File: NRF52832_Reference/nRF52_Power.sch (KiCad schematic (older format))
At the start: 37 parts

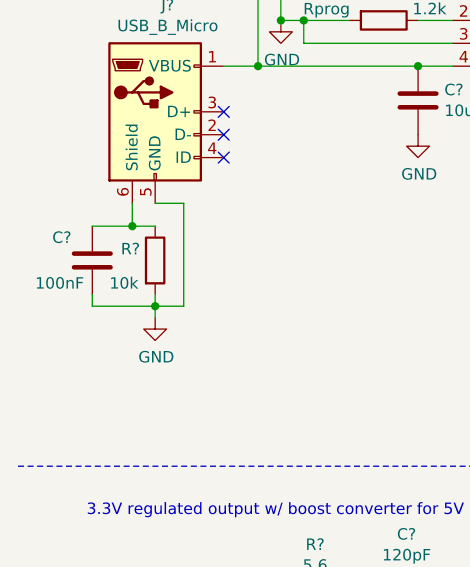
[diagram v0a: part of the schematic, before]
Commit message: Added footprint for LCD and finished footprint assignments for LCD components.
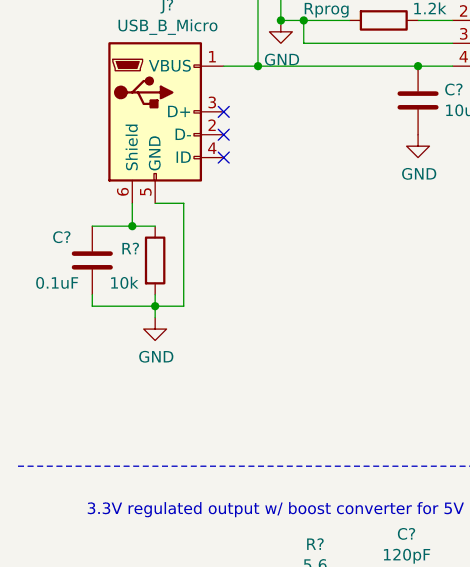
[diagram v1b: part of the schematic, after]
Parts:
- C?: value 100nF -> 0.1uF
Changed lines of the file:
@@
 P 825 3000
 F 0 "C?" H 650 3100 50  0000 L CNN
-F 1 "100nF" H 575 2900 50  0000 L CNN
+F 1 "0.1uF" H 575 2900 50  0000 L CNN
 F 2 "Capacitor_SMD:C_0603_1608Metric_Pad1.05x0.95mm_HandSolder" H 863 2850 50  0001 C CNN
 F 3 "~" H 825 3000 50  0001 C CNN

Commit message: Finished foorprint assignments for GPIO pins, LEDs, and button.
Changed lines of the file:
@@
 	0    1    1    0
 $EndComp
-Text Label 6200 2150 0    50   ~ 0
-V+
-Text Label 700  4900 0    50   ~ 0
-V+
 Wire Wire Line
 	1600 4900 1500 4900
@@
 Wire Wire Line
 	825  3200 1100 3200
+Text GLabel 6200 2150 2    50   Output ~ 0
+V+
+Text GLabel 700  4900 0    50   Input ~ 0
+V+
 $EndSCHEMATC

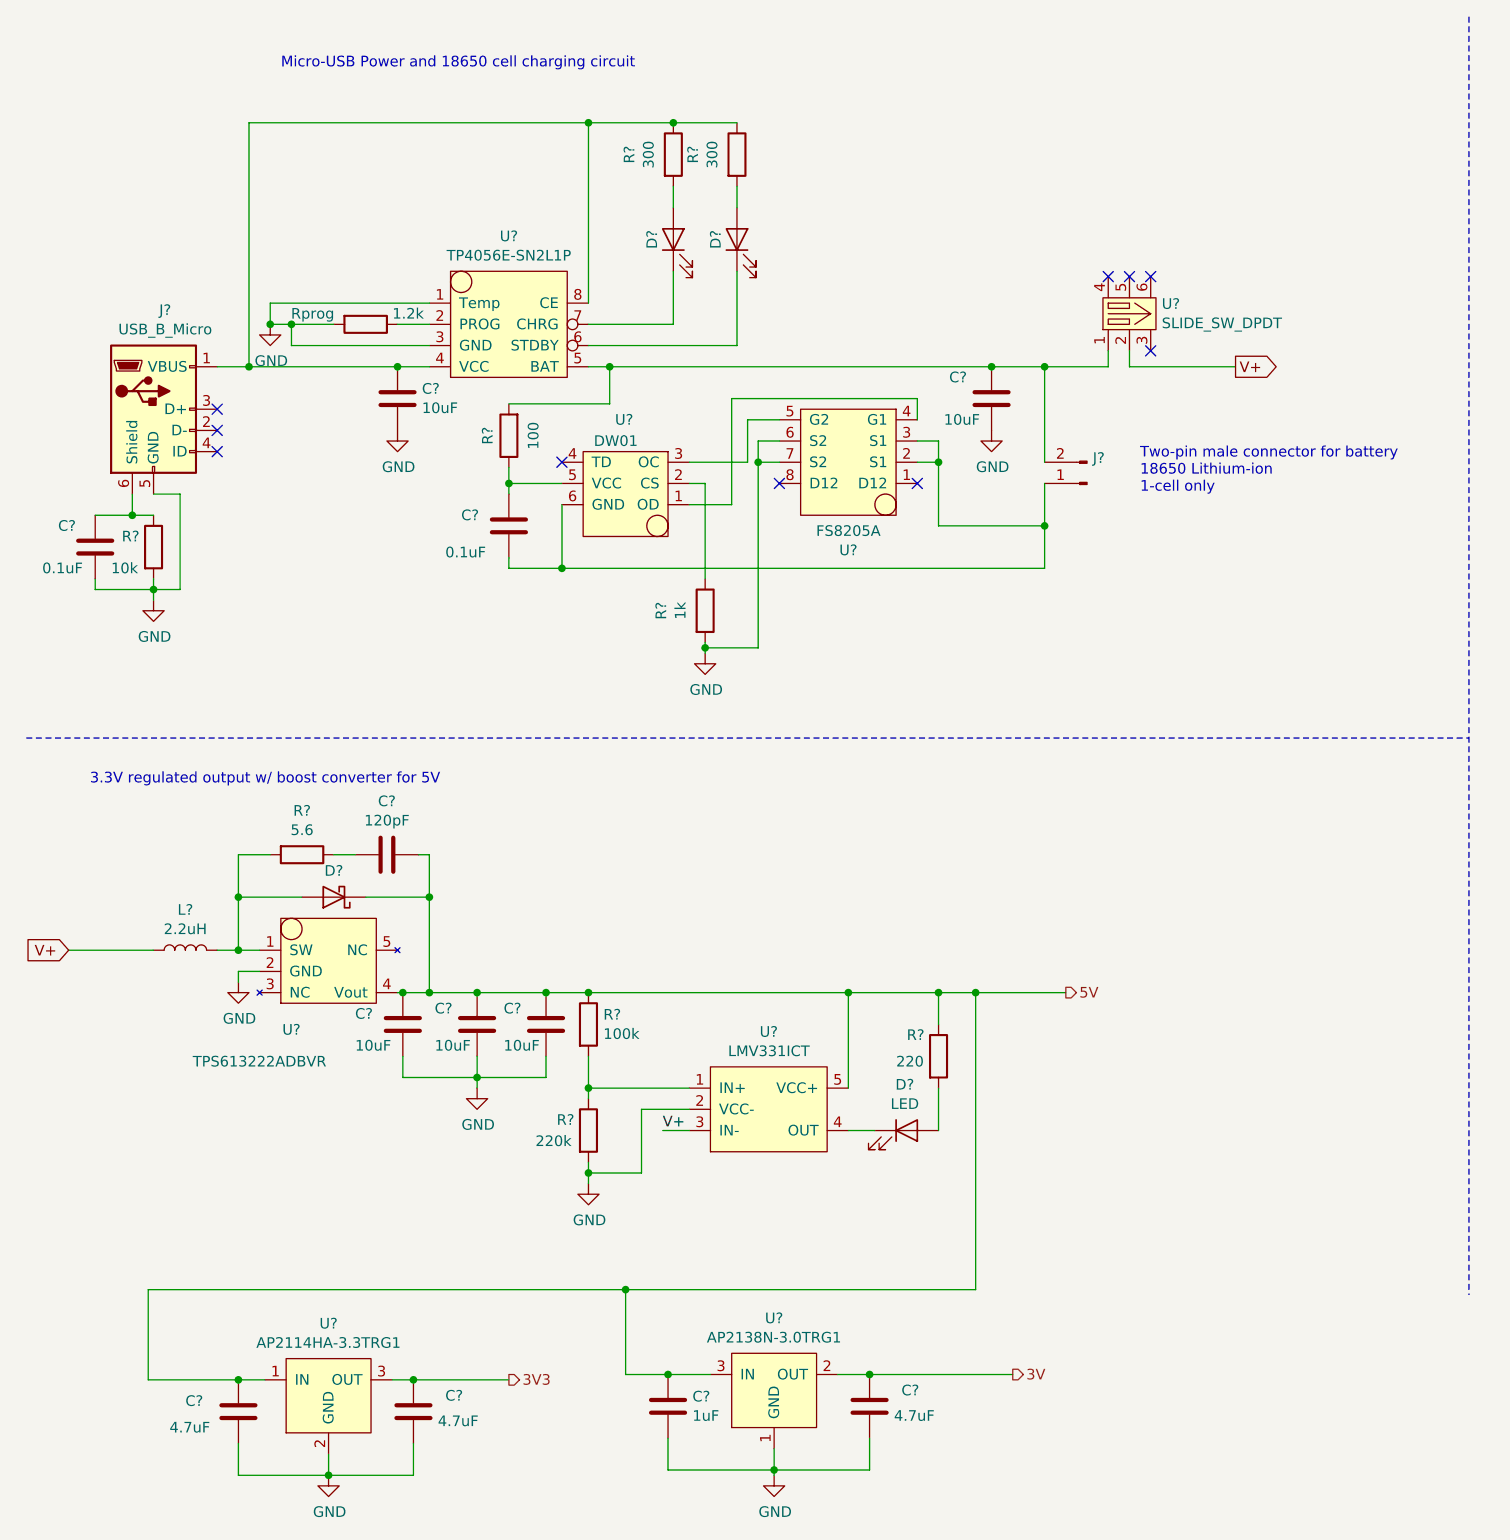
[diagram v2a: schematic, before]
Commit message: Finished footprint assignments for NRF52 base components
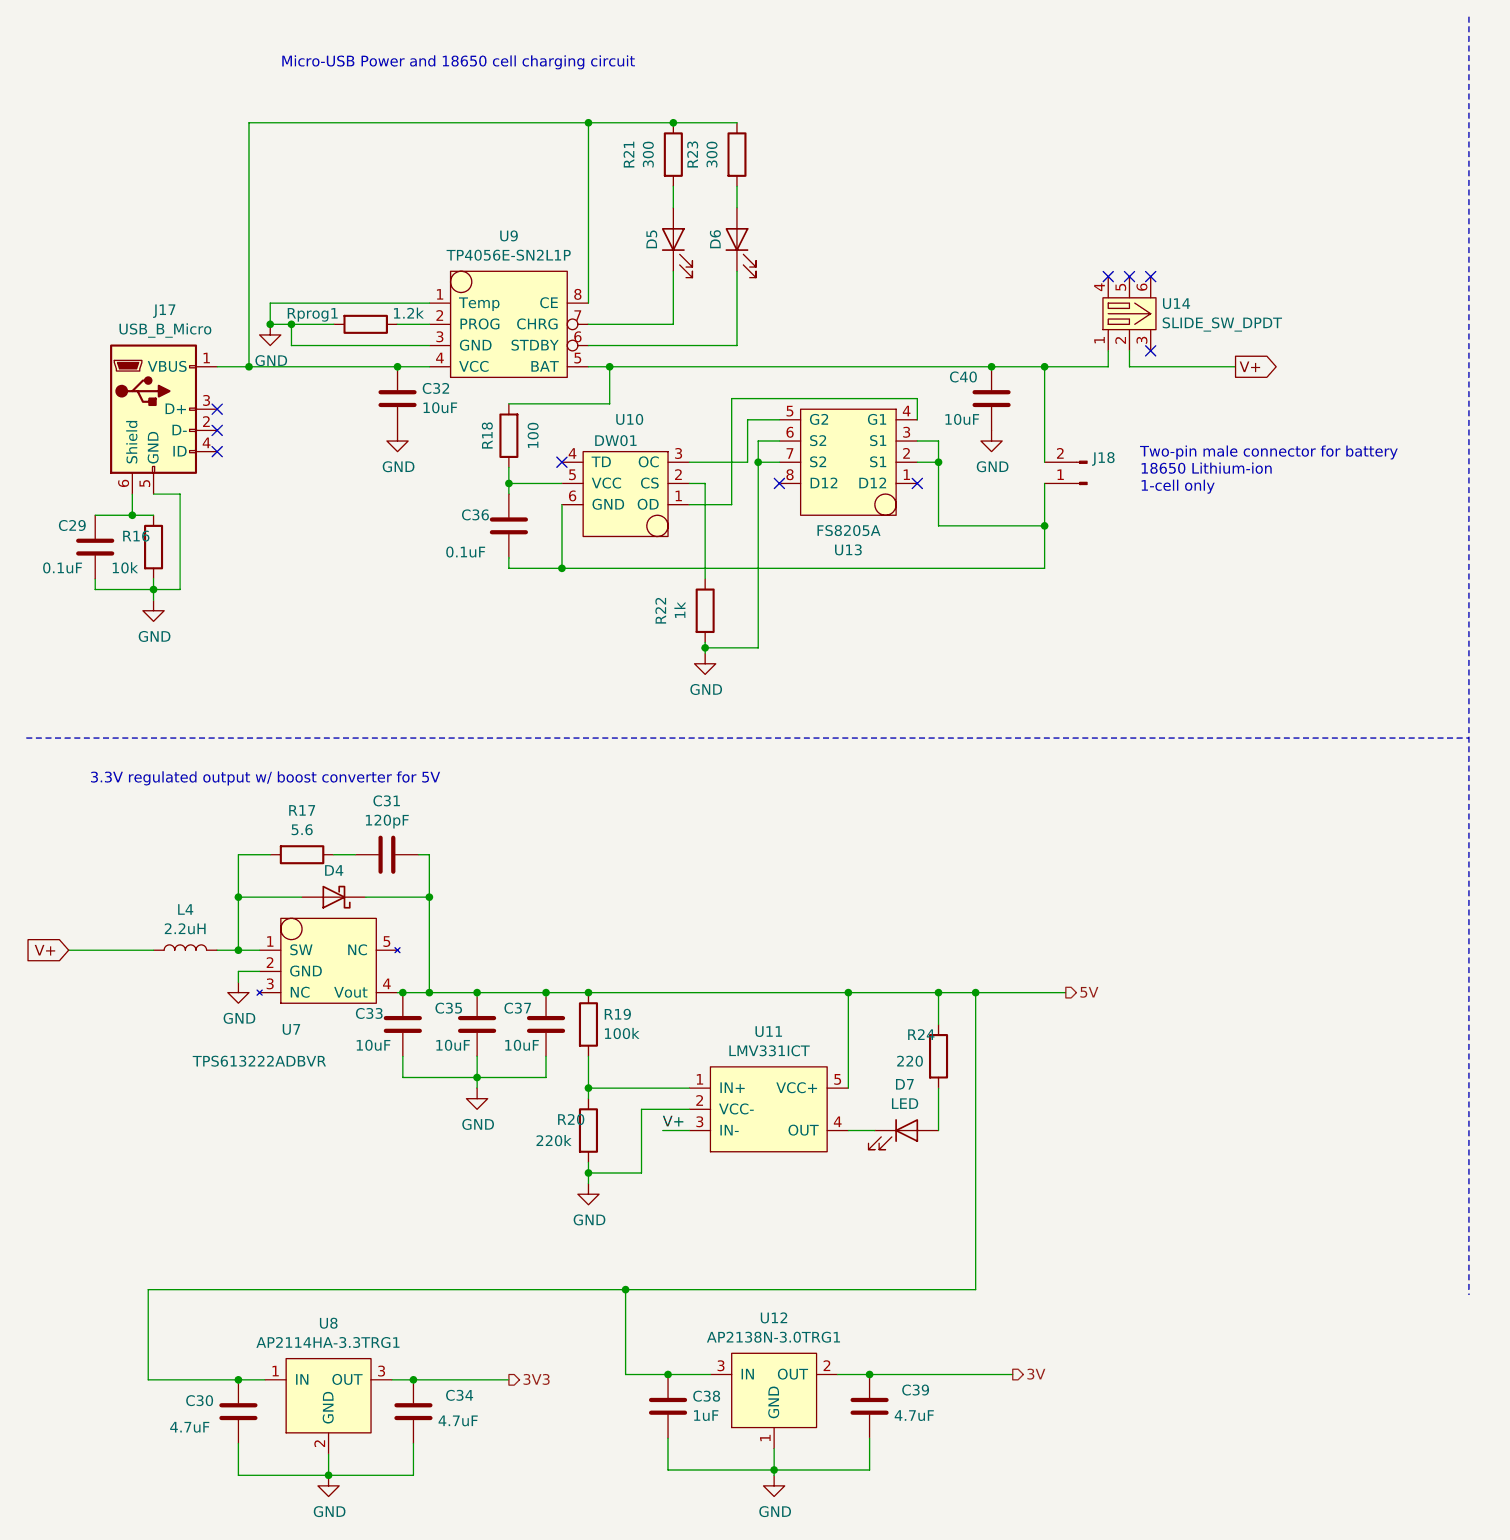
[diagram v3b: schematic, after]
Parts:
- gave numbers to parts that had none: 36
- renumbered Rprog to Rprog1

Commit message: Updated component placement for PCB layout
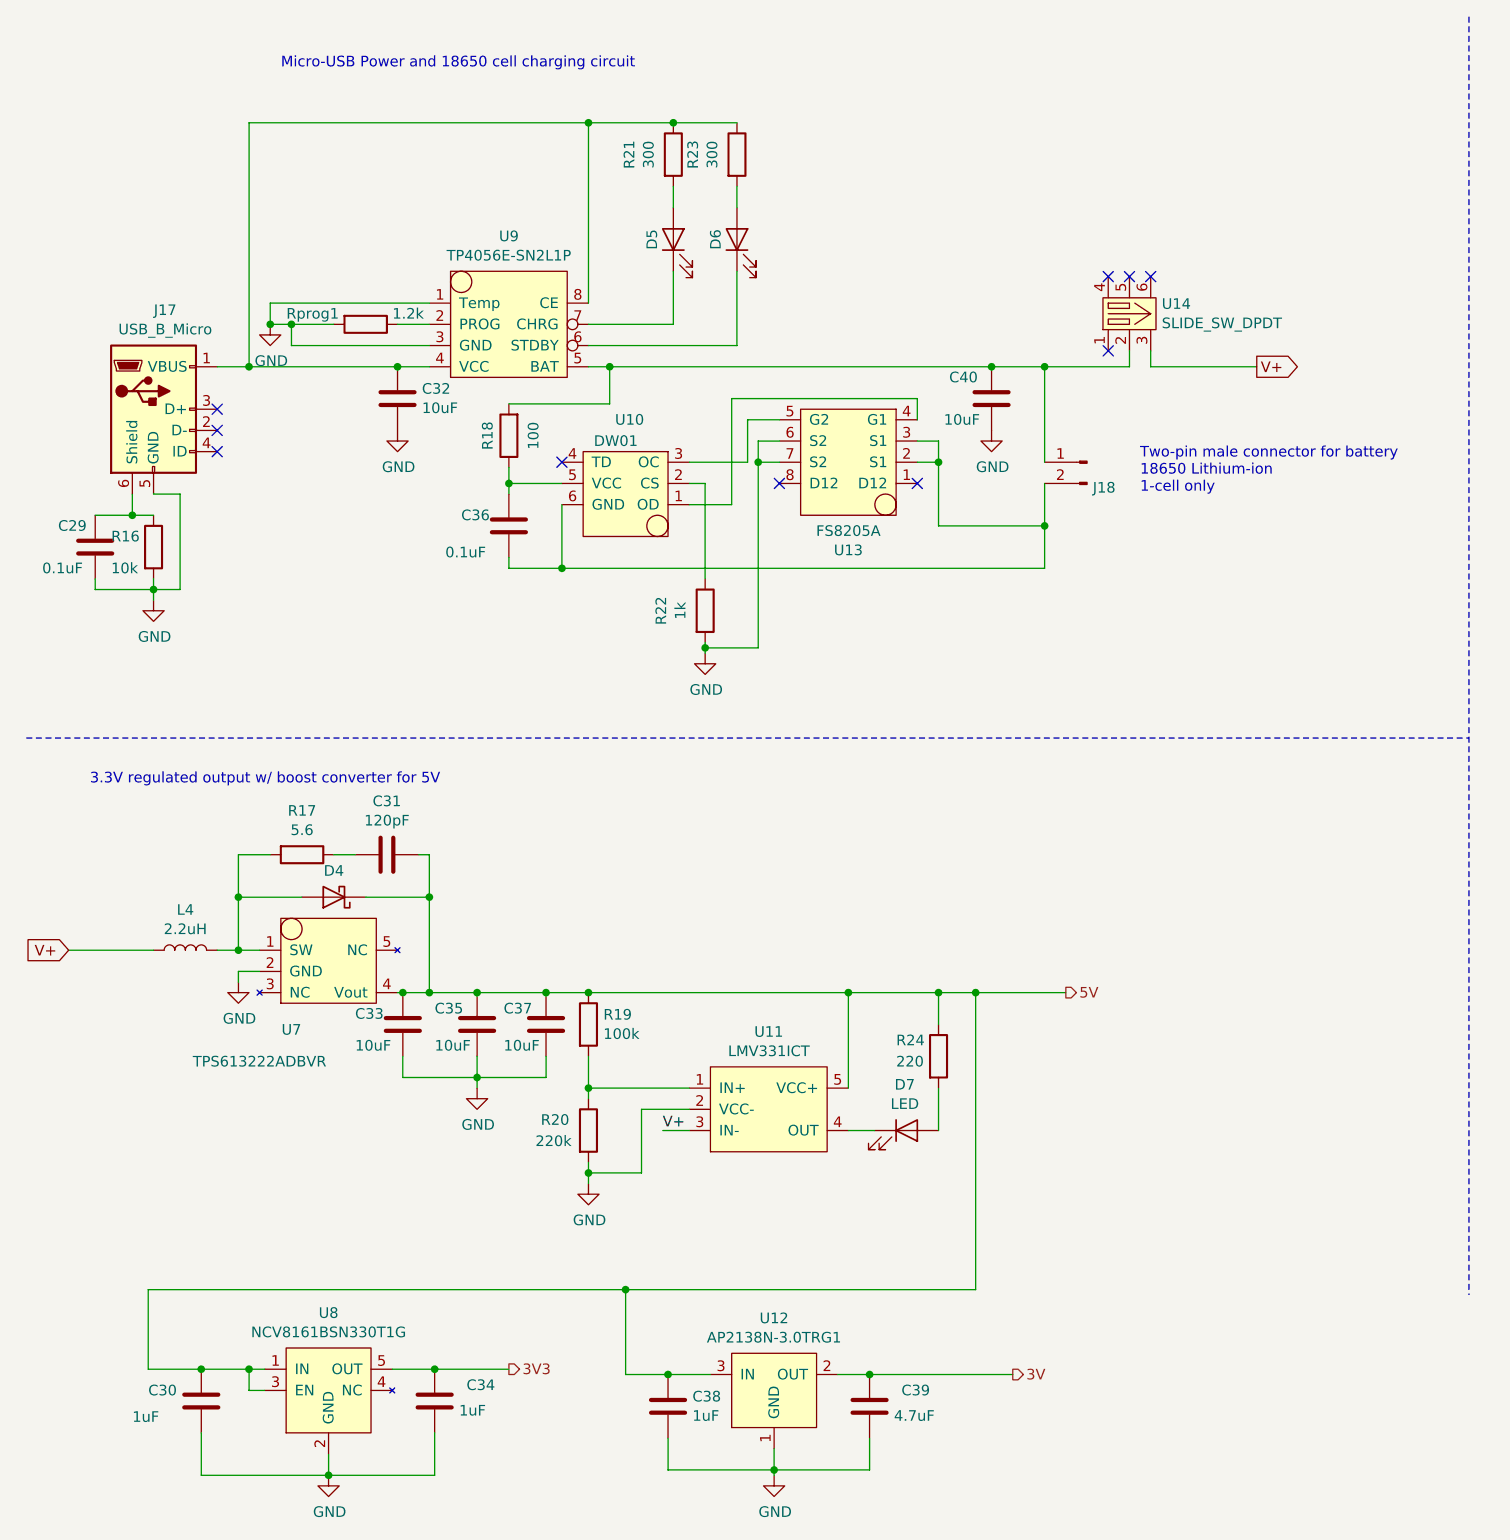
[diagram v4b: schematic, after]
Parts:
- removed U8: AP2114HA-3.3TRG1, Package_TO_SOT_SMD:SOT-223-3_TabPin2, symbol Project_Libary:AP2114HA-3.3TRG1
- added U8: NCV8161BSN330T1G, Package_SO:TSOP-5_1.65x3.05mm_P0.95mm, symbol Project_Libary:NCV8161BSN330T1G
- C30, C34: value 4.7uF -> 1uF
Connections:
- net 3V3: now also U8.5 (OUT)
- net 5V: now also U8.1 (IN), U8.3 (EN)
- net GND: now also U8.2 (GND)
- net V+: now also U14.3; no longer U14.2
- net at C36.2, U10.6 (GND), U13.2 (S1)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: now also J18.2 (Pin_2); no longer J18.1 (Pin_1)
- net at C40.1, R18.2, U9.5 (BAT): now also J18.1 (Pin_1), U14.2; no longer J18.2 (Pin_2), U14.1
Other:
- moved on the sheet: C30, C34
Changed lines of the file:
@@
 L Connector:Conn_01x02_Male J18
 U 1 1 5BF32F95
-P 5500 2700
-F 0 "J18" H 5473 2580 50  0000 R CNN
-F 1 "Conn_01x02_Male" H 5473 2671 50  0001 R CNN
-F 2 "Connector_PinHeader_2.54mm:PinHeader_1x02_P2.54mm_Horizontal" H 5500 2700 50  0001 C CNN
-F 3 "~" H 5500 2700 50  0001 C CNN
-	1    5500 2700
-	-1   0    0    1
+P 5500 2600
+F 0 "J18" H 5473 2480 50  0000 R CNN
+F 1 "Conn_01x02_Male" H 5473 2571 50  0001 R CNN
+F 2 "Connector_PinHeader_2.54mm:PinHeader_1x02_P2.54mm_Horizontal" H 5500 2600 50  0001 C CNN
+F 3 "~" H 5500 2600 50  0001 C CNN
+	1    5500 2600
+	-1   0    0    -1
 $EndComp
 $Comp
@@
 L Device:C C?
 U 1 1 5BF5917C
-P 1500 7075
+P 1325 7025
 AR Path="/5BF5917C" Ref="C?"  Part="1"
 AR Path="/5BF31556/5BF5917C" Ref="C30"  Part="1"
-F 0 "C30" H 1250 7125 50  0000 L CNN
-F 1 "4.7uF" H 1175 7000 50  0000 L CNN
-F 2 "Capacitor_SMD:C_0603_1608Metric_Pad1.05x0.95mm_HandSolder" H 1538 6925 50  0001 C CNN
-F 3 "~" H 1500 7075 50  0001 C CNN
-	1    1500 7075
+F 0 "C30" H 1075 7075 50  0000 L CNN
+F 1 "1uF" H 1000 6950 50  0000 L CNN
+F 2 "Capacitor_SMD:C_0603_1608Metric_Pad1.05x0.95mm_HandSolder" H 1363 6875 50  0001 C CNN
+F 3 "~" H 1325 7025 50  0001 C CNN
+	1    1325 7025
 	1    0    0    -1
 $EndComp
@@
 Wire Wire Line
 	2400 4650 2400 4450
-Text HLabel 2775 6925 2    50   Output ~ 0
+Text HLabel 2775 6875 2    50   Output ~ 0
 3V3
 Text HLabel 5400 5100 2    50   Output ~ 0
@@
 U 1 1 5C0A072D
 P 3150 5750
-F 0 "R20" H 3000 5800 50  0000 L CNN
+F 0 "R20" H 2925 5800 50  0000 L CNN
 F 1 "220k" H 2900 5700 50  0000 L CNN
 F 2 "Resistor_SMD:R_0603_1608Metric_Pad1.05x0.95mm_HandSolder" V 3080 5750 50  0001 C CNN
@@
 L Device:C C?
 U 1 1 5BF59183
-P 2325 7075
+P 2425 7025
 AR Path="/5BF59183" Ref="C?"  Part="1"
 AR Path="/5BF31556/5BF59183" Ref="C34"  Part="1"
-F 0 "C34" H 2475 7150 50  0000 L CNN
-F 1 "4.7uF" H 2440 7030 50  0000 L CNN
-F 2 "Capacitor_SMD:C_0603_1608Metric_Pad1.05x0.95mm_HandSolder" H 2363 6925 50  0001 C CNN
-F 3 "~" H 2325 7075 50  0001 C CNN
-	1    2325 7075
+F 0 "C34" H 2575 7100 50  0000 L CNN
+F 1 "1uF" H 2540 6980 50  0000 L CNN
+F 2 "Capacitor_SMD:C_0603_1608Metric_Pad1.05x0.95mm_HandSolder" H 2463 6875 50  0001 C CNN
+F 3 "~" H 2425 7025 50  0001 C CNN
+	1    2425 7025
 	1    0    0    -1
 $EndComp
@@
 U 1 1 5C0C9CDB
 P 4800 5400
-F 0 "R24" H 4650 5500 50  0000 L CNN
+F 0 "R24" H 4600 5475 50  0000 L CNN
 F 1 "220" H 4600 5375 50  0000 L CNN
 F 2 "Resistor_SMD:R_0603_1608Metric_Pad1.05x0.95mm_HandSolder" V 4730 5400 50  0001 C CNN
@@
 Wire Wire Line
 	4800 5250 4800 5100
-$Comp
-L Project_Libary:AP2114HA-3.3TRG1 U8
-U 1 1 5C0D7B49
-P 1925 6975
-F 0 "U8" H 1925 7290 50  0000 C CNN
-F 1 "AP2114HA-3.3TRG1" H 1925 7199 50  0000 C CNN
-F 2 "Package_TO_SOT_SMD:SOT-223-3_TabPin2" H 1925 7225 50  0001 C CNN
-F 3 "" H 1925 7225 50  0001 C CNN
-	1    1925 6975
-	1    0    0    -1
-$EndComp
-Wire Wire Line
-	2325 7375 1925 7375
-Wire Wire Line
-	1500 7225 1500 7375
-Wire Wire Line
-	1500 7375 1925 7375
 Connection ~ 1925 7375
 Wire Wire Line
 	1925 7275 1925 7375
-Wire Wire Line
-	1625 6925 1500 6925
-Connection ~ 1500 6925
-Wire Wire Line
-	1500 6925 1075 6925
-Wire Wire Line
-	2225 6925 2325 6925
-Connection ~ 2325 6925
 Wire Notes Line
 	7300 500  7300 6525
@@
 	3150 5950 3150 6000
 Wire Wire Line
-	1075 6500 1075 6925
-Wire Wire Line
 	4975 5100 4975 6500
 $Comp
@@
 	1    0    0    -1
 $EndComp
-Wire Wire Line
-	2325 7375 2325 7225
 $Comp
 L Device:C C38
@@
 $EndComp
 Wire Wire Line
-	5600 2150 5600 2075
-Wire Wire Line
-	5300 2150 5600 2150
-Wire Wire Line
-	5700 2150 5700 2075
-Wire Wire Line
-	5700 2150 6200 2150
-NoConn ~ 5800 2075
+	5800 2150 5800 2075
+Wire Wire Line
+	5800 2150 6300 2150
+NoConn ~ 5600 2075
 NoConn ~ 5800 1725
 NoConn ~ 5700 1725
 NoConn ~ 5600 1725
-Wire Wire Line
-	2325 6925 2775 6925
 Connection ~ 3325 6500
 Wire Wire Line
@@
 U 1 1 5C0E61D3
 P 1100 3000
-F 0 "R16" H 950 3050 50  0000 L CNN
+F 0 "R16" H 900 3050 50  0000 L CNN
 F 1 "10k" H 900 2900 50  0000 L CNN
 F 2 "Resistor_SMD:R_0603_1608Metric_Pad1.05x0.95mm_HandSolder" V 1030 3000 50  0001 C CNN
@@
 Wire Wire Line
 	825  3200 1100 3200
-Text GLabel 6200 2150 2    50   Output ~ 0
+Text GLabel 6300 2150 2    50   Output ~ 0
 V+
 Text GLabel 700  4900 0    50   Input ~ 0
 V+
+Wire Wire Line
+	5700 2150 5700 2075
+Wire Wire Line
+	5300 2150 5700 2150
+$Comp
+L Project_Libary:NCV8161BSN330T1G U8
+U 1 1 5C1429EA
+P 1925 6925
+F 0 "U8" H 1925 7240 50  0000 C CNN
+F 1 "NCV8161BSN330T1G" H 1925 7149 50  0000 C CNN
+F 2 "Package_SO:TSOP-5_1.65x3.05mm_P0.95mm" H 1825 7375 50  0001 C CNN
+F 3 "" H 1825 7375 50  0001 C CNN
+	1    1925 6925
+	1    0    0    -1
+$EndComp
+Connection ~ 2425 6875
+Wire Wire Line
+	2425 6875 2775 6875
+Wire Wire Line
+	1075 6500 1075 6875
+Wire Wire Line
+	1075 6875 1325 6875
+Connection ~ 1325 6875
+Wire Wire Line
+	1325 6875 1550 6875
+Wire Wire Line
+	1325 7175 1325 7375
+Wire Wire Line
+	1325 7375 1925 7375
+Wire Wire Line
+	2425 7375 2425 7175
+Wire Wire Line
+	1925 7375 2425 7375
+Wire Wire Line
+	2225 6875 2425 6875
+Wire Wire Line
+	1625 6975 1550 6975
+Wire Wire Line
+	1550 6975 1550 6875
+Connection ~ 1550 6875
+Wire Wire Line
+	1550 6875 1625 6875
 $EndSCHEMATC
